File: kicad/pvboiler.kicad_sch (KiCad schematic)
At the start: 32 parts, among them J1 Conn_01x04, J2 Screw_Terminal_01x04, J3 Conn_01x04, J4 Screw_Terminal_01x03, U1 MOC3021M, U2 H11AA1, U3 IRM-03-5

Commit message: changed: Increase opto cap size footprint changed: Pcb version bump to rev1
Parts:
- C8: footprint Capacitor_THT:C_Rect_L7.2mm_W2.5mm_P5.00mm -> Capacitor_THT:C_Rect_L10.0mm_W4.0mm_P7.50mm_MKS4
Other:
- title: ESP PVBoiler -> ESP PvBoiler
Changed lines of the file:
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@@
 	(paper "A4")
 	(title_block
-		(title "ESP PVBoiler")
-		(rev "0")
+		(title "ESP PvBoiler")
+		(rev "1")
 		(company "Arno van Amersfoort (Arnova)")
 	)
@@
 			)
 		)
-		(property "Footprint" "Capacitor_THT:C_Rect_L7.2mm_W2.5mm_P5.00mm"
+		(property "Footprint" "Capacitor_THT:C_Rect_L10.0mm_W4.0mm_P7.50mm_MKS4"
 			(at 147.0152 33.02 0)
 			(hide yes)

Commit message: added: Schematic pdf added: Pictures
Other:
- note added: "BTA25/BTA40 Triac"
- note added: "From Schaffner FN2060-16-06 Line Filter"
- note added: "| 230VAC N | 230VAC L"
- note added: "| MT1 | G | MT2"
- note removed: "230VAC L"
- note removed: "230VAC N"
- note removed: "From Schaffner FN2060-16-06 Line Filter | |"
- note removed: "MT1 G MT2"
- note removed: "| BTA25/BTA40 Triac | |"
- moved on the sheet: C2, C4, C6, C7, C8, F1, J1, J2, J3, J4, R1, R10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

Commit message: updated: Some tweaks in KiCAD schematic / pcb
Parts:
- added R12, R13, R14, R15: 22E, Resistor_SMD:R_1206_3216Metric, symbol Device:R
- R6, R7: value 10K -> 2K2
- R8, R9: value 0E -> 10E
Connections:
- net I2C_SCL: now also R12.2, R14.2; no longer J1.3 (Pin_3), J3.3 (Pin_3)
- net I2C_SDA: now also R13.2, R15.2; no longer J1.4 (Pin_4), J3.4 (Pin_4)
- new net: J1.3 (Pin_3), R14.1
- new net: J1.4 (Pin_4), R15.1
- new net: J3.3 (Pin_3), R12.1
- new net: J3.4 (Pin_4), R13.1
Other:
- moved on the sheet: C6, C7, R6, R7, R8, R9

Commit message: changed: Expose ESP8266 D0 on extra tp
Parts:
- added R16, R17: 4K7, Resistor_SMD:R_1206_3216Metric, symbol Device:R
- added TP5: TestPoint, TestPoint:TestPoint_THTPad_D2.0mm_Drill1.0mm, symbol Connector:TestPoint
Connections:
- net +3.3V_1: now also R16.2, R17.2
- net AUX_GPIO: now also A1.30 (D0), R16.1, TP5.1; no longer A1.22 (D6), TP4.1
- new net ONE_WIRE: A1.22 (D6), R17.1, TP4.1
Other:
- moved on the sheet: C10, C9, TP1, TP2, TP3, TP4

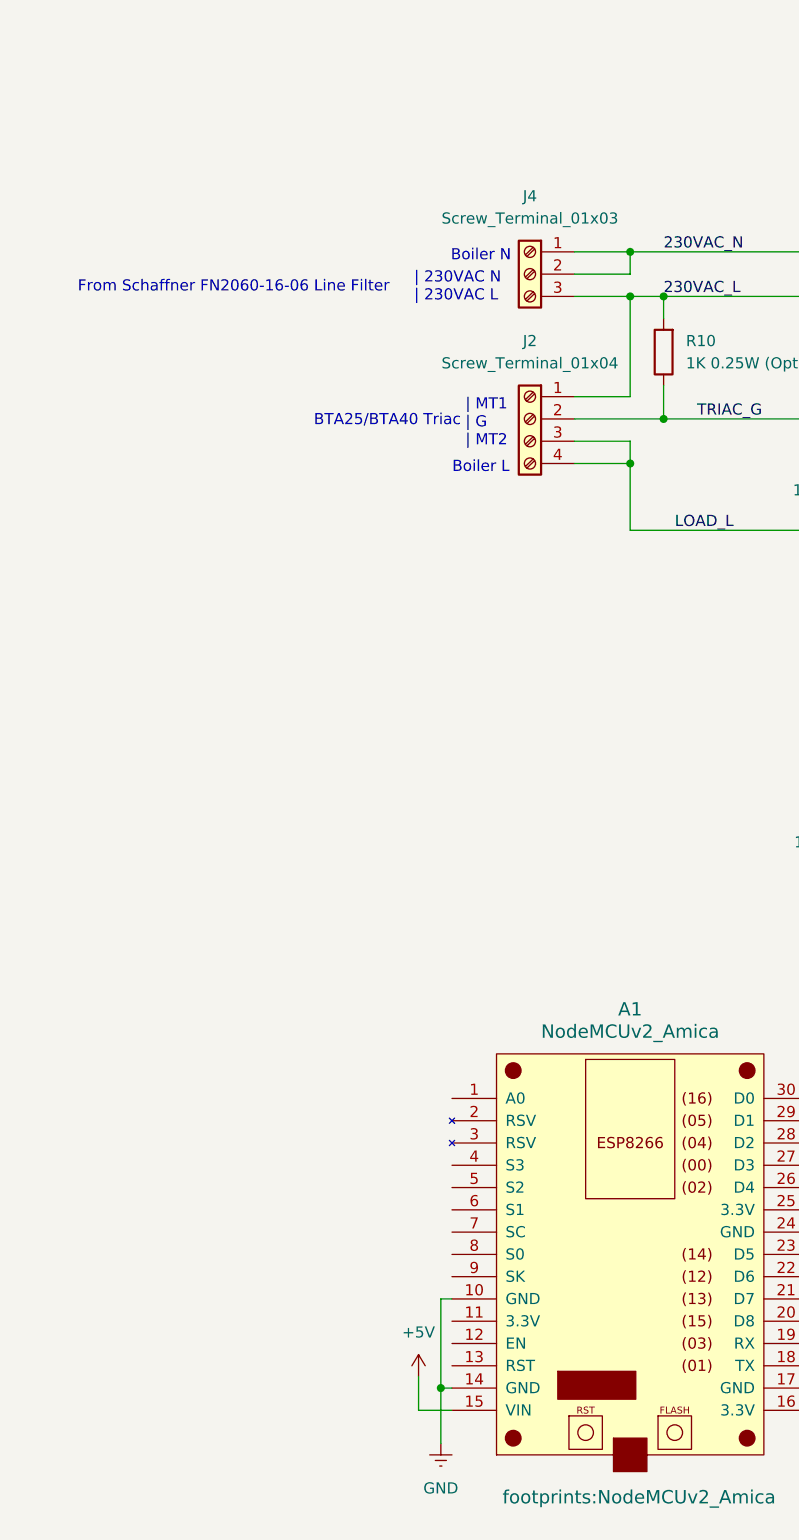
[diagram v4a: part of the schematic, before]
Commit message: changed: Add (future) CT connection for A0 changed: Improve schematic
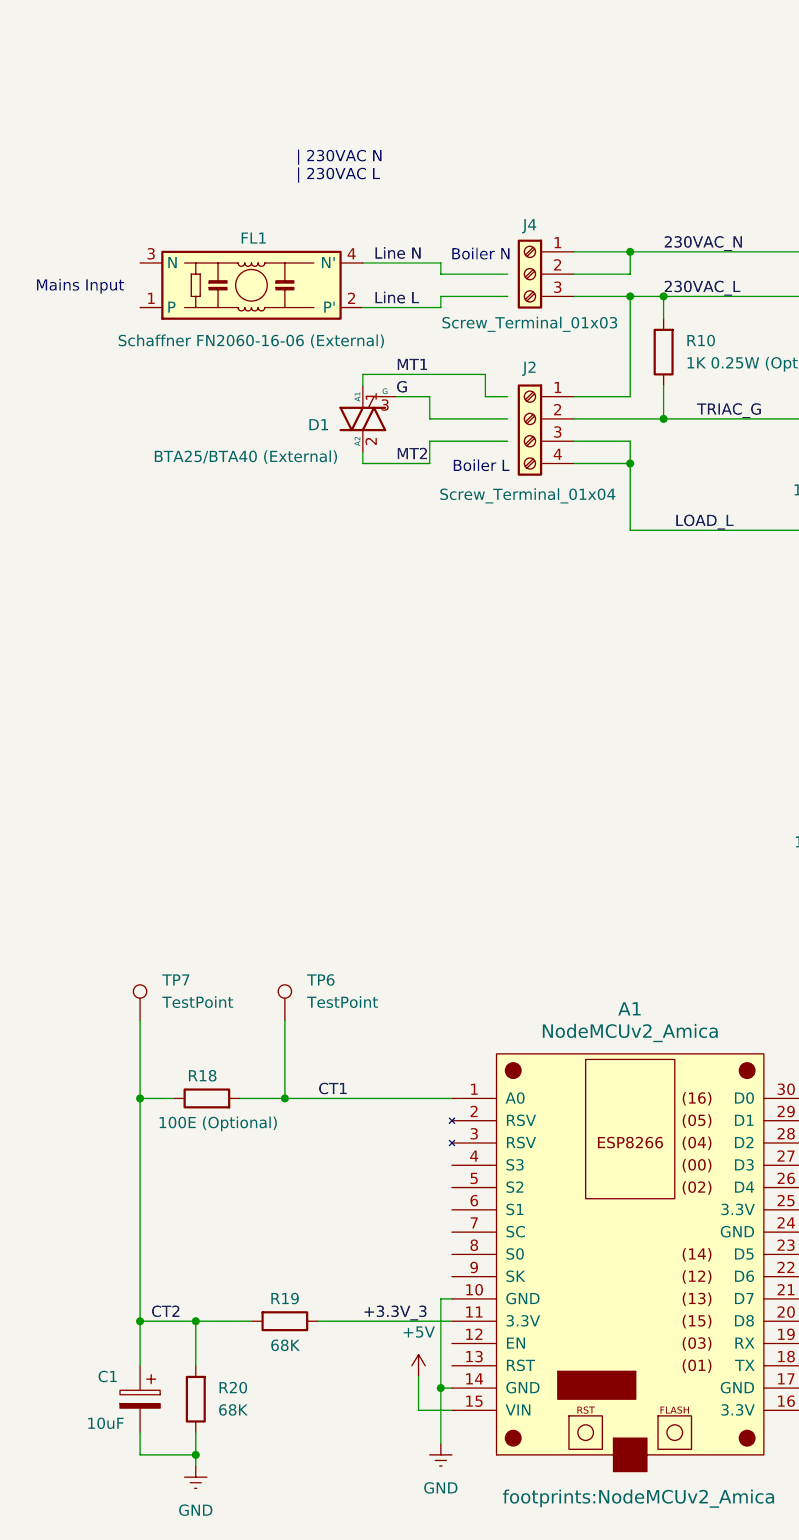
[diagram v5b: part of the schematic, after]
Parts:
- added C1: 10uF, Capacitor_Tantalum_SMD:CP_EIA-3216-18_Kemet-A_HandSolder, symbol Device:C_Polarized
- added D1: BTA25/BTA40 (External), Package_LCC:PLCC-44_16.6x16.6mm_P1.27mm, symbol Triac_Thyristor:Generic_Triac_A1A2G
- added FL1: Schaffner FN2060-16-06 (External), Filter:Filter_FILTERCON_1FPxx, symbol Filter:1FP41-4R
- added R18: 100E (Optional), Resistor_SMD:R_1206_3216Metric, symbol Device:R
- added R19, R20: 68K, Resistor_SMD:R_1206_3216Metric, symbol Device:R
- added TP6, TP7: TestPoint, TestPoint:TestPoint_THTPad_D2.0mm_Drill1.0mm, symbol Connector:TestPoint
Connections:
- net GND: now also C1.2, R20.1
- net CT1: now reaches A1.1 (A0)
- net CT1: now also R18.2, TP6.1
- net +3.3V_3: now reaches A1.11 (3.3V)
- net +3.3V_3: now also R19.1
- new net CT2: C1.1, R18.1, R19.2, R20.2, TP7.1
- new net G: D1.3 (G)
- new net Line L: FL1.2 (P')
- new net Line N: FL1.4 (N')
- new net MT1: D1.1 (A1)
- new net MT2: D1.2 (A2)
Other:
- note added: "Mains Input"
- note removed: "BTA25/BTA40 Triac"
- note removed: "From Schaffner FN2060-16-06 Line Filter"
- note removed: "| MT1 | G | MT2"

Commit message: updated: Tweaks in schematic/PCB
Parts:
- added R21, R22: 10E, Resistor_SMD:R_1206_3216Metric, symbol Device:R
- added R23: 100E, Resistor_SMD:R_1206_3216Metric, symbol Device:R
- R16, R17: value 4K7 -> 2K2
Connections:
- net +3.3V_1: now also R22.2; no longer C10.1, TP2.1
- net +5V: now also R21.2; no longer C9.1, TP1.1
- net ONE_WIRE: now also R23.1; no longer TP4.1
- new net: C9.1, R21.1, TP1.1
- new net: C10.1, R22.1, TP2.1
- new net: R23.2, TP4.1
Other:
- moved on the sheet: R17

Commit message: updated: Kicad schematic/pcb
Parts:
- R16: value 2K2 -> 10K
- TP1, TP2, TP3, TP4, TP5, TP6, TP7: footprint TestPoint:TestPoint_THTPad_D2.0mm_Drill1.0mm -> TestPoint:TestPoint_THTPad_D2.5mm_Drill1.2mm
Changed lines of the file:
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@@
 			)
 		)
-		(property "Footprint" "TestPoint:TestPoint_THTPad_D2.0mm_Drill1.0mm"
+		(property "Footprint" "TestPoint:TestPoint_THTPad_D2.5mm_Drill1.2mm"
 			(at 123.19 132.08 0)
 			(hide yes)
@@
 			)
 		)
-		(property "Footprint" "TestPoint:TestPoint_THTPad_D2.0mm_Drill1.0mm"
+		(property "Footprint" "TestPoint:TestPoint_THTPad_D2.5mm_Drill1.2mm"
 			(at 137.16 104.14 0)
 			(hide yes)
@@
 		(fields_autoplaced yes)
 		(property "Reference" "R17"
-			(at 149.86 140.9699 0)
+			(at 149.86 140.97 0)
 			(show_name no)
 			(do_not_autoplace no)
@@
 		)
 		(property "Value" "2K2"
-			(at 149.86 143.5099 0)
+			(at 149.86 143.51 0)
 			(show_name no)
 			(do_not_autoplace no)
@@
 		(fields_autoplaced yes)
 		(property "Reference" "R16"
-			(at 128.27 130.8099 0)
+			(at 128.27 130.81 0)
 			(show_name no)
 			(do_not_autoplace no)
@@
 			)
 		)
-		(property "Value" "2K2"
-			(at 128.27 133.3499 0)
+		(property "Value" "10K"
+			(at 128.27 133.35 0)
 			(show_name no)
 			(do_not_autoplace no)
@@
 			)
 		)
-		(property "Footprint" "TestPoint:TestPoint_THTPad_D2.0mm_Drill1.0mm"
+		(property "Footprint" "TestPoint:TestPoint_THTPad_D2.5mm_Drill1.2mm"
 			(at 48.26 129.54 0)
 			(hide yes)
@@
 			)
 		)
-		(property "Footprint" "TestPoint:TestPoint_THTPad_D2.0mm_Drill1.0mm"
+		(property "Footprint" "TestPoint:TestPoint_THTPad_D2.5mm_Drill1.2mm"
 			(at 31.75 129.54 0)
 			(hide yes)
@@
 			)
 		)
-		(property "Footprint" "TestPoint:TestPoint_THTPad_D2.0mm_Drill1.0mm"
+		(property "Footprint" "TestPoint:TestPoint_THTPad_D2.5mm_Drill1.2mm"
 			(at 120.65 104.14 0)
 			(hide yes)
@@
 			)
 		)
-		(property "Footprint" "TestPoint:TestPoint_THTPad_D2.0mm_Drill1.0mm"
+		(property "Footprint" "TestPoint:TestPoint_THTPad_D2.5mm_Drill1.2mm"
 			(at 138.43 115.57 0)
 			(hide yes)
@@
 			)
 		)
-		(property "Footprint" "TestPoint:TestPoint_THTPad_D2.0mm_Drill1.0mm"
+		(property "Footprint" "TestPoint:TestPoint_THTPad_D2.5mm_Drill1.2mm"
 			(at 138.43 132.08 0)
 			(hide yes)
